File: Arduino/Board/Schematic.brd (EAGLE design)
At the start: 82.6 x 70.5 mm, 43 parts, among them Q1 2N7002E, Q2 2N7002E, Q3 2N7002E

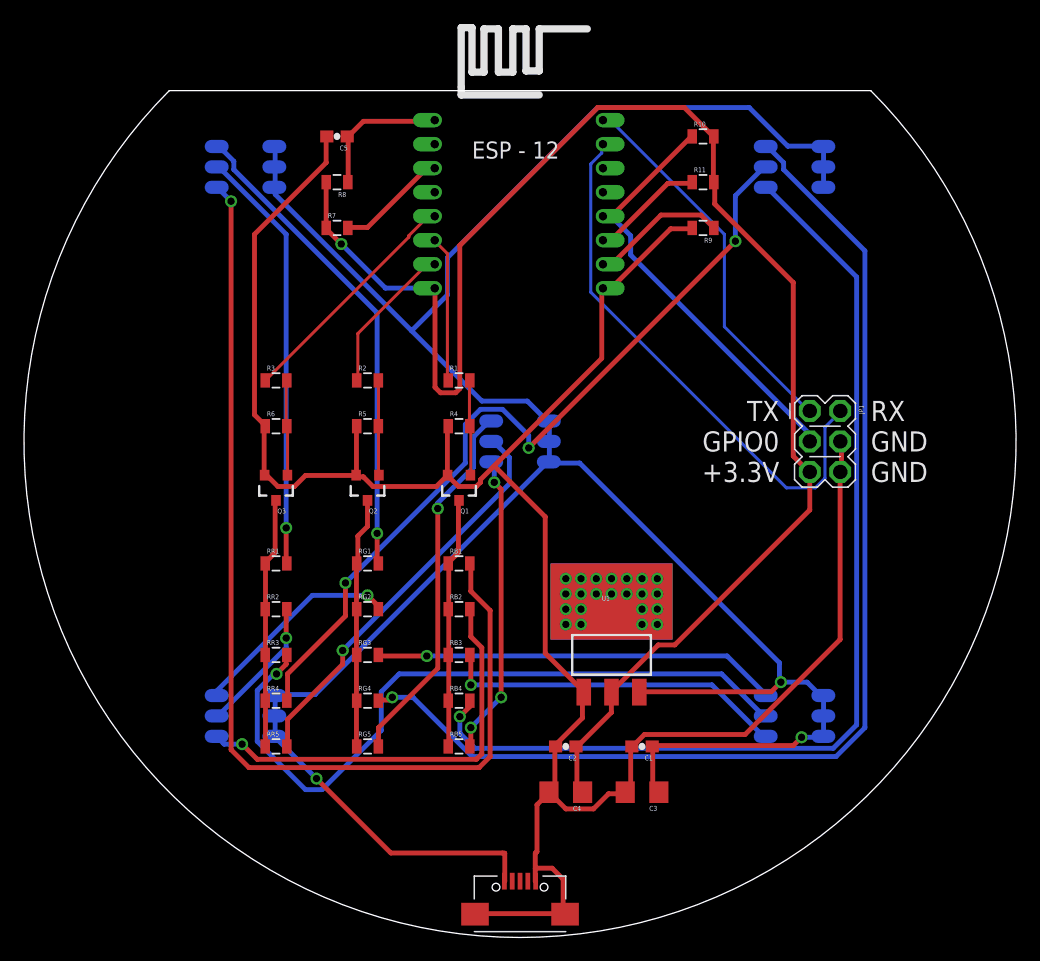
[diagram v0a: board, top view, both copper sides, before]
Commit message: pcb upgrade
changed:
- bigger (size) resistors for LEDs
- changed MOSFETs for more power
- added ambient light sensors
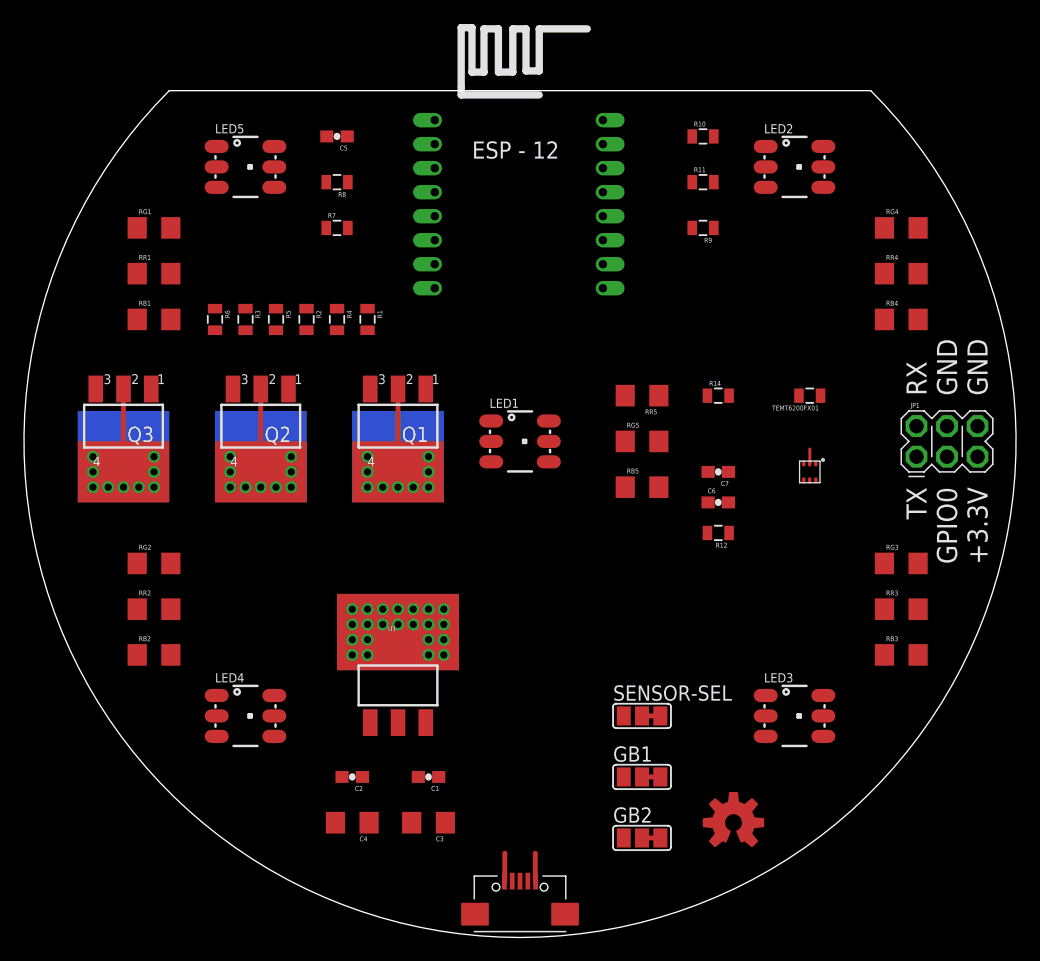
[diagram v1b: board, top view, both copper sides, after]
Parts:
- added C6, C7: ?, SparkFun-Capacitors:0603-CAP
- added GB1, GB2, SENSOR-SEL: (no value), SparkFun-Passives:PAD-JUMPER-3-2OF3_NC_BY_TRACE_YES_SILK_LARGE
- added LOGO1: OSHW-LOGOM-COPPER, SparkFun-Aesthetics:OSHW-LOGO-M_COPPER
- added R12: ?, SparkFun-Passives:0805
- added R14: 10K, SparkFun-Passives:0805
- added TEMT6200FX01: (no value), SparkFun-Passives:0805
- added U$3: NOA1212, MCustom:505AL
- Q1, Q2, Q3: value 2N7002E -> NTF3055L108; device SparkFun-DiscreteSemi:SOT23-3 -> zetex:SOT223
- RB1, RB2, RB3, RB4, RB5, RG1, RG2, RG3, RG4, RG5, RR1, RR2, RR3, RR4, RR5: value 91 -> 18; device SparkFun-Passives:0805 -> SparkFun-Passives:1206
- moved RR4 63.1 mm to (82.5, 64.8)
- moved RG4 59.4 mm to (82.5, 68.6)
- moved RR3 52.2 mm to (82.5, 36.8)
- moved RB4 48.6 mm to (82.5, 61.0)
- moved RG3 45.1 mm to (82.5, 40.6)
- moved RR5 42.2 mm to (61.0, 54.6), turned to 180 degrees
- moved RB3 36.8 mm to (82.5, 33.0)
- moved RG5 34.2 mm to (61.0, 50.8)
- moved RG1 33.1 mm to (20.3, 68.6)
- moved RB1 32.5 mm to (20.3, 61.0)
- moved RB5 26.4 mm to (61.0, 47.0)
- moved RR1 26.2 mm to (20.3, 64.8)
- moved RB2 25.7 mm to (20.3, 33.0)
- moved RG2 18.2 mm to (20.3, 40.6)
- moved C1 18.0 mm to (43.2, 22.9)
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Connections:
- new net ADC: SENSOR-SEL.2, U$1.ADC
- new net N$1111: C6.1, R12.2, SENSOR-SEL.1, U$3.P$6
- new net N$51: GB2.2, U$3.P$4
- new net N$54: GB1.2, U$3.P$3
- net GND: now also C6.2, C7.2, GB1.1, GB2.1, Q1.3, Q2.3, Q3.3, R12.1, R14.1, R14.2, SENSOR-SEL.3, TEMT6200FX01.2, U$3.P$2; no longer Q1.2, Q2.2, Q3.2
- net N$5: now also Q1.2, Q1.4; no longer Q1.3
- net N$7: now also Q2.2, Q2.4; no longer Q2.3
- net N$9: now also Q3.2, Q3.4; no longer Q3.3
- net VCC: now also C7.1, GB1.3, GB2.3, TEMT6200FX01.1, U$3.P$1
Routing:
- net N$2: track 212.6 -> 2.36 mm, vias 3 -> 0
- net GND: track 191.1 -> 3.56 mm
- net VCC: track 131.6 -> 0.00 mm, vias 1 -> 0
- net N$16: track 95.6 -> 0.00 mm, vias 1 -> 0
- net N$1: track 86.7 -> 0.00 mm, vias 1 -> 0
- net N$15: track 85.4 -> 0.00 mm, vias 1 -> 0
- net N$17: track 68.6 -> 0.00 mm, vias 3 -> 0
- net N$14: track 59.7 -> 0.00 mm, vias 1 -> 0
- net N$53: track 45.5 -> 0.00 mm
- net N$4: track 40.4 -> 0.00 mm, vias 1 -> 0
- net N$46: track 36.6 -> 0.00 mm
- net N$6: track 35.6 -> 0.00 mm, vias 1 -> 0
- net N$8: track 35.5 -> 0.00 mm, vias 1 -> 0
- net N$19: track 33.8 -> 0.00 mm, vias 1 -> 0
- net N$13: track 33.7 -> 0.00 mm, vias 1 -> 0
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
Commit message: added buzzer
added buzzer and holes for air flow
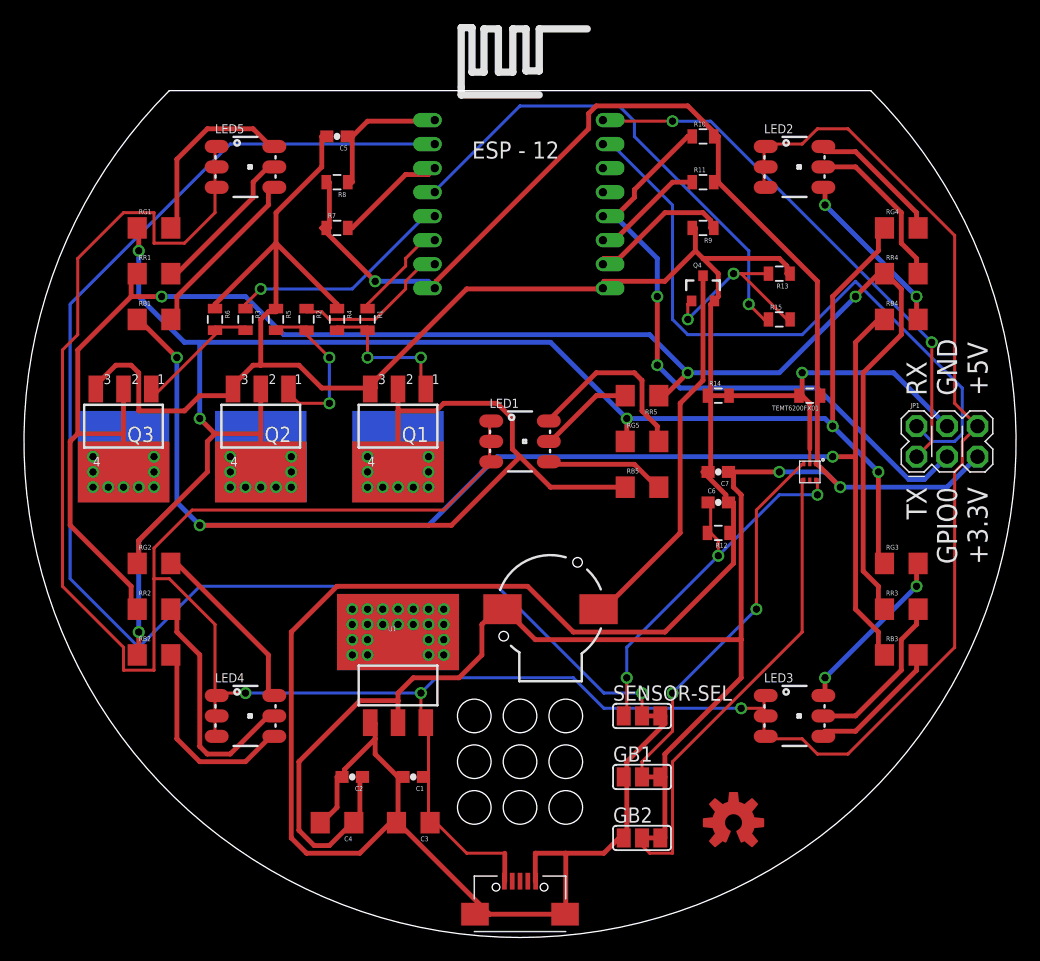
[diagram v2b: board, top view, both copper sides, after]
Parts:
- added Q4: MOSFET-NCHANNELAO3404A, SparkFun-DiscreteSemi:SOT23-3
- added R13: 10K, SparkFun-Passives:0805
- added R15: 100, SparkFun-Passives:0805
- added SG1: BUZZERSMD2, SparkFun-Electromechanical:BUZZER-CCV
- moved C1 1.27 mm to (41.9, 22.9)
- moved C3 1.27 mm to (41.9, 19.1)
- moved C4 1.27 mm to (35.6, 19.1)
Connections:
- removed net N$2: C1.1, C3.1, LED1.1, LED1.2, LED1.3, LED2.1, LED2.2, LED2.3, LED3.1, LED3.2, LED3.3, LED4.1, LED4.2, LED4.3, LED5.1, LED5.2, LED5.3, U$2.VBUS, U1.3
- new net N$82: Q4.1, R13.2, R15.2
- new net N$83: Q4.3, SG1.+
- new net SIGNAL-BUZZ: R15.1, U$1.GPIO16
- new net VBUS: C1.1, C3.1, JP1.P$6, LED1.1, LED1.2, LED1.3, LED2.1, LED2.2, LED2.3, LED3.1, LED3.2, LED3.3, LED4.1, LED4.2, LED4.3, LED5.1, LED5.2, LED5.3, U$2.VBUS, U1.3
- net GND: now also Q4.2, R13.1; no longer JP1.P$6
- net VCC: now also SG1.-
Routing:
- net GND: track 3.56 -> 304.6 mm, vias 0 -> 1
- net VBUS: track 0.00 -> 274.3 mm, vias 0 -> 3
- net VCC: track 0.00 -> 202.1 mm, vias 0 -> 3
- net N$5: track 6.20 -> 179.8 mm, vias 0 -> 4
- net N$9: track 6.20 -> 146.1 mm, vias 0 -> 3
- net N$7: track 6.20 -> 134.0 mm, vias 0 -> 5
- net ADC: track 0.00 -> 116.4 mm, vias 0 -> 1
- net N$53: track 0.00 -> 56.0 mm
- net N$46: track 0.00 -> 54.5 mm, vias 0 -> 2
- net N$52: track 0.00 -> 45.1 mm, vias 0 -> 2
- net SIGNAL-BUZZ: track 0.00 -> 41.5 mm, vias 0 -> 1
- net N$51: track 0.00 -> 39.2 mm
- net N$1111: track 0.00 -> 33.7 mm, vias 0 -> 3
- net N$83: track 0.00 -> 31.8 mm
- net N$54: track 0.00 -> 31.7 mm, vias 0 -> 2
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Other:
- board text added: "+5V"

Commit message: updated the board design
updated to the requirements in the https://trello.com/c/WxGEJiPR
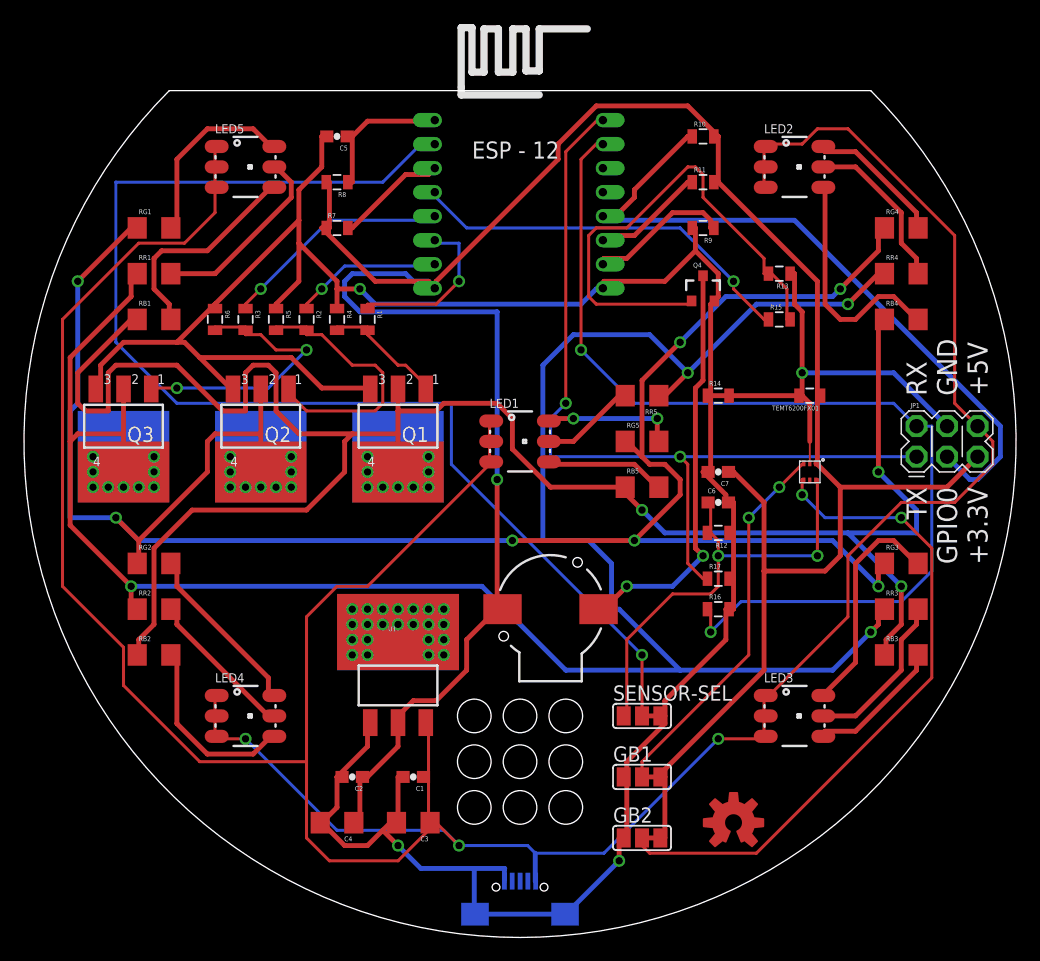
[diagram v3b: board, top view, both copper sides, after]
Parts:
- added R16, R17: 10K, SparkFun-Passives:0805
- flipped U$2 to the bottom
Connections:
- net GND: now also R16.2, R17.2
- net N$52: now also R17.1
- net N$53: now also R16.1
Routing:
- net GND: track 304.6 -> 254.9 mm, vias 1 -> 4
- net N$9: track 146.1 -> 182.7 mm, vias 3 -> 4
- net N$7: track 134.0 -> 170.5 mm, vias 5 -> 7
- net N$53: track 56.0 -> 84.8 mm, vias 0 -> 2
- net N$52: track 45.1 -> 71.9 mm
- net N$82: track 15.6 -> 41.8 mm, vias 2 -> 0
- net N$51: track 39.2 -> 55.9 mm, vias 0 -> 2
- net VCC: track 202.1 -> 216.4 mm, vias 3 -> 1
- net ADC: track 116.4 -> 103.9 mm
- net N$22: track 11.2 -> 23.3 mm, vias 0 -> 2
- net N$5: track 179.8 -> 168.8 mm, vias 4 -> 3
- net SIGNAL-BUZZ: track 41.5 -> 32.7 mm
- net N$21: track 14.0 -> 22.7 mm, vias 2 -> 0
- net N$11: track 20.5 -> 13.0 mm
- net N$15: track 14.3 -> 19.6 mm, vias 2 -> 0
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
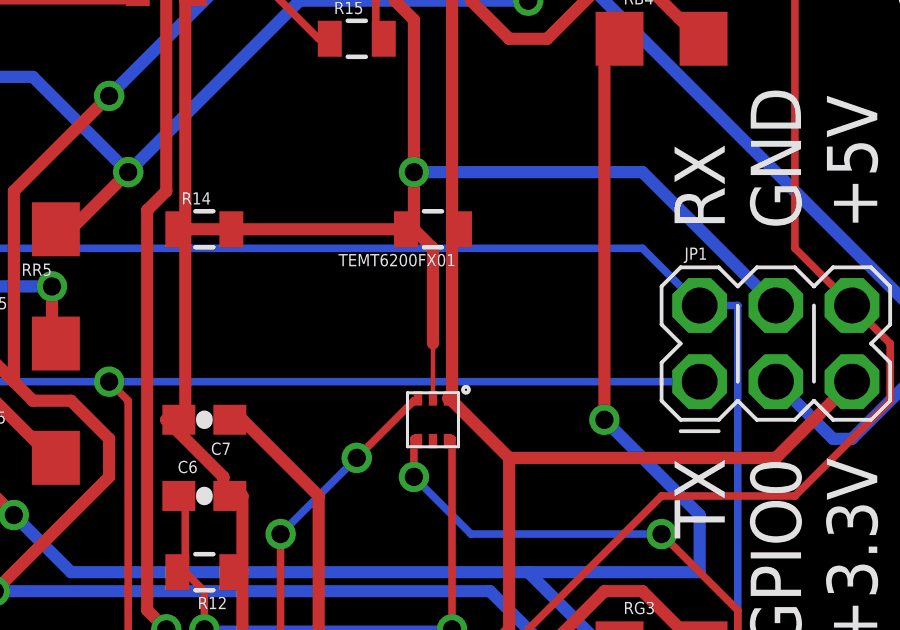
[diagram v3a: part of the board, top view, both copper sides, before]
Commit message: small fixes to the board.
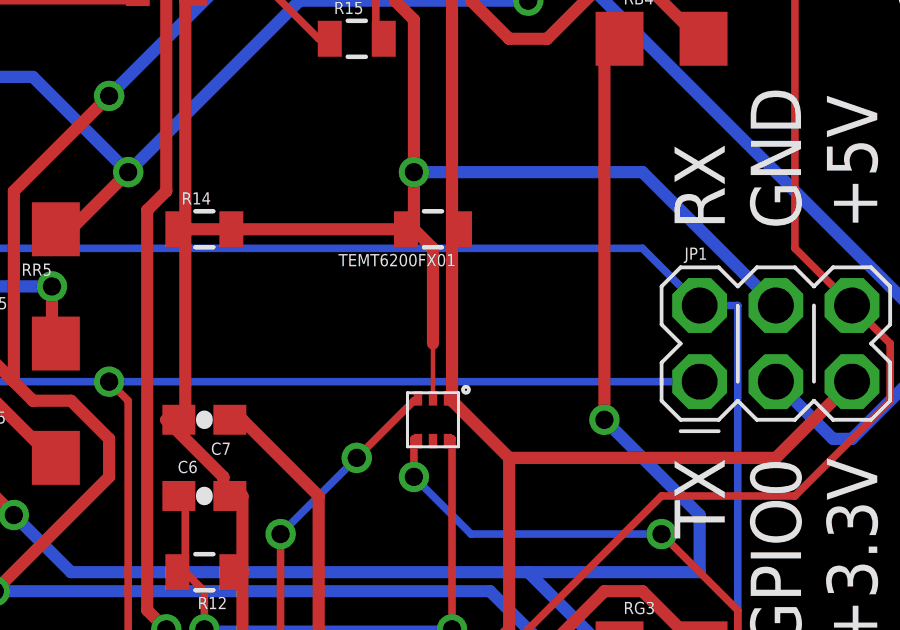
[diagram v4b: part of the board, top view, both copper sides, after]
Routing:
- net VCC: track 216.4 -> 217.0 mm
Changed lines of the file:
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@@
 <wire x1="34.29" y1="68.58" x2="34.66" y2="68.58" width="0.4064" layer="1"/>
 <wire x1="67.31" y1="76.2" x2="67.31" y2="72.39" width="0.4064" layer="1"/>
-<wire x1="75.565" y1="54.61" x2="75.565" y2="48.895" width="0.4064" layer="1"/>
+<wire x1="75.565" y1="54.61" x2="75.565" y2="49.53" width="0.4064" layer="1"/>
+<wire x1="75.565" y1="49.53" x2="75.565" y2="48.895" width="0.4064" layer="1"/>
 <wire x1="75.565" y1="64.135" x2="67.31" y2="72.39" width="0.4064" layer="1"/>
 <wire x1="75.565" y1="54.61" x2="75.565" y2="64.135" width="0.4064" layer="1"/>
@@
 <wire x1="77.47" y1="46.99" x2="86.36" y2="46.99" width="0.4064" layer="1"/>
 <wire x1="75.565" y1="48.895" x2="77.47" y2="46.99" width="0.4064" layer="1"/>
-<wire x1="75.565" y1="48.895" x2="75.43" y2="48.97" width="0.4064" layer="1"/>
 <wire x1="53.975" y1="74.295" x2="43.815" y2="64.135" width="0.4064" layer="1"/>
 <wire x1="53.975" y1="75.565" x2="53.975" y2="74.295" width="0.4064" layer="1"/>
@@
 <wire x1="77.47" y1="46.99" x2="77.47" y2="41.275" width="0.4064" layer="1"/>
 <via x="48.895" y="47.625" extent="1-16" drill="0.6096"/>
+<wire x1="75.43" y1="48.97" x2="75.565" y2="48.97" width="0.1524" layer="1"/>
+<wire x1="75.565" y1="48.97" x2="75.565" y2="49.53" width="0.1524" layer="1"/>
 </signal>
 <signal name="N$5" class="1">

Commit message: updated board (Rev. 3)
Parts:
- removed C6, C7: ?, SparkFun-Capacitors:0603-CAP
- removed GB1, GB2, SENSOR-SEL: (no value), SparkFun-Passives:PAD-JUMPER-3-2OF3_NC_BY_TRACE_YES_SILK_LARGE
- removed R12: ?, SparkFun-Passives:0805
- removed U$3: NOA1212, MCustom:505AL
- Q1, Q2, Q3: device zetex:SOT223 -> MCustom:SOT223HEAT
- moved C2 2.54 mm to (34.3, 22.9)
- moved C4 1.27 mm to (34.3, 19.1)
- moved C1 1.27 mm to (40.6, 22.9)
- moved C3 1.27 mm to (40.6, 19.1)
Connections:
- removed net N$1111: C6.1, R12.2, SENSOR-SEL.1, U$3.P$6
- removed net N$51: GB2.2, U$3.P$4
- removed net N$54: GB1.2, U$3.P$3
- net ADC: now also R14.2, TEMT6200FX01.2; no longer SENSOR-SEL.2
- net GND: no longer C6.2, C7.2, GB1.1, GB2.1, R12.1, R14.2, SENSOR-SEL.3, TEMT6200FX01.2, U$3.P$2
- net N$5: now also Q1.P$1, Q1.P$10, Q1.P$11, Q1.P$12, Q1.P$13, Q1.P$14, Q1.P$15, Q1.P$16, Q1.P$17, Q1.P$18, Q1.P$19, Q1.P$2, Q1.P$3, Q1.P$4, Q1.P$5, Q1.P$6, Q1.P$7, Q1.P$8, Q1.P$9
- net N$7: now also Q2.P$1, Q2.P$10, Q2.P$11, Q2.P$12, Q2.P$13, Q2.P$14, Q2.P$15, Q2.P$16, Q2.P$17, Q2.P$18, Q2.P$19, Q2.P$2, Q2.P$3, Q2.P$4, Q2.P$5, Q2.P$6, Q2.P$7, Q2.P$8, Q2.P$9
- net N$9: now also Q3.P$1, Q3.P$10, Q3.P$11, Q3.P$12, Q3.P$13, Q3.P$14, Q3.P$15, Q3.P$16, Q3.P$17, Q3.P$18, Q3.P$19, Q3.P$2, Q3.P$3, Q3.P$4, Q3.P$5, Q3.P$6, Q3.P$7, Q3.P$8, Q3.P$9
- net VCC: no longer C7.1, GB1.3, GB2.3, U$3.P$1
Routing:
- net N$9: track 182.7 -> 243.0 mm, vias 4 -> 0
- net N$51: track 55.9 -> 0.00 mm, vias 2 -> 0
- net ADC: track 103.9 -> 55.0 mm, vias 1 -> 0
- net VBUS: track 277.5 -> 231.0 mm, vias 3 -> 6
- net N$7: track 170.5 -> 213.1 mm, vias 7 -> 3
- net N$1111: track 38.6 -> 0.00 mm, vias 2 -> 0
- net N$54: track 31.7 -> 0.00 mm, vias 2 -> 0
- net N$82: track 41.8 -> 12.1 mm
- net N$53: track 84.8 -> 62.3 mm
- net VCC: track 217.0 -> 197.4 mm, vias 1 -> 5
- net N$21: track 22.7 -> 7.43 mm
- net N$22: track 23.3 -> 9.90 mm, vias 2 -> 0
- net N$46: track 59.7 -> 50.2 mm, vias 0 -> 1
- net GND: track 254.9 -> 263.1 mm
- net SIGNAL-BLU: track 14.1 -> 8.36 mm, vias 1 -> 0
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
